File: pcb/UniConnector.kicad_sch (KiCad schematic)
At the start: 1 part

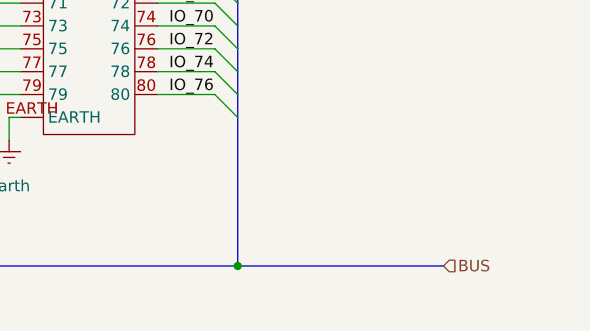
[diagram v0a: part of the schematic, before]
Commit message: Add junction and bus entries to UniConnector schematic
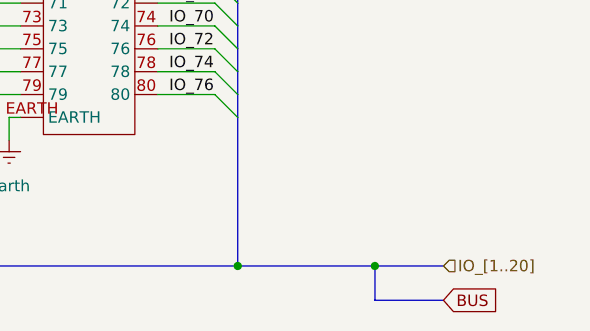
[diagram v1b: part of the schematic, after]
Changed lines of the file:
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@@
 		(color 0 0 0 0)
 	)
+	(junction
+		(at 138.43 146.05)
+		(diameter 0)
+		(color 0 0 0 0)
+	)
 	(bus_entry
 		(at 90.17 124.46)
@@
 		)
 	)
+	(bus
+		(pts
+			(xy 138.43 149.86) (xy 146.05 149.86)
+		)
+		(stroke
+			(width 0)
+			(type default)
+		)
+	)
 	(wire
 		(pts
@@
 		)
 	)
+	(bus
+		(pts
+			(xy 138.43 146.05) (xy 146.05 146.05)
+		)
+		(stroke
+			(width 0)
+			(type default)
+		)
+	)
 	(wire
 		(pts
@@
 	(bus
 		(pts
-			(xy 123.19 146.05) (xy 146.05 146.05)
+			(xy 123.19 146.05) (xy 138.43 146.05)
 		)
 		(stroke
@@
 		(pts
 			(xy 114.3 40.64) (xy 120.65 40.64)
+		)
+		(stroke
+			(width 0)
+			(type default)
+		)
+	)
+	(bus
+		(pts
+			(xy 138.43 146.05) (xy 138.43 149.86)
 		)
 		(stroke
@@
 		)
 	)
-	(hierarchical_label "BUS"
+	(global_label "BUS"
+		(shape input)
+		(at 146.05 149.86 0)
+		(fields_autoplaced yes)
+		(effects
+			(font
+				(size 1.27 1.27)
+			)
+			(justify left)
+		)
+		(property "Intersheetrefs" "${INTERSHEET_REFS}"
+			(at 152.191 149.86 0)
+			(effects
+				(font
+					(size 1.27 1.27)
+				)
+				(justify left)
+				(hide yes)
+			)
+		)
+	)
+	(hierarchical_label "IO_[1..20]"
 		(shape input)
 		(at 146.05 146.05 0)

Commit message: UniConnector new traces
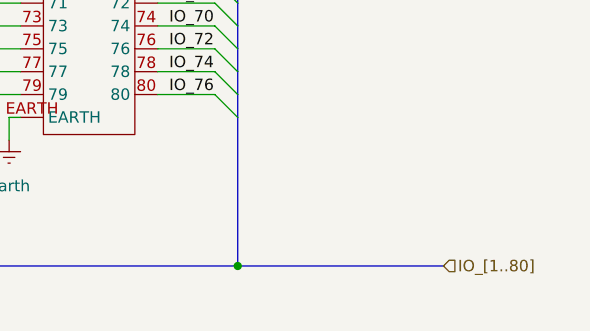
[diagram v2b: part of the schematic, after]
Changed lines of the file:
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@@
 		(color 0 0 0 0)
 	)
-	(junction
-		(at 138.43 146.05)
-		(diameter 0)
-		(color 0 0 0 0)
-	)
 	(bus_entry
 		(at 90.17 124.46)
@@
 		)
 	)
-	(bus
-		(pts
-			(xy 138.43 149.86) (xy 146.05 149.86)
-		)
-		(stroke
-			(width 0)
-			(type default)
-		)
-	)
 	(wire
 		(pts
@@
 		)
 	)
-	(bus
-		(pts
-			(xy 138.43 146.05) (xy 146.05 146.05)
-		)
-		(stroke
-			(width 0)
-			(type default)
-		)
-	)
 	(wire
 		(pts
@@
 	(bus
 		(pts
-			(xy 123.19 146.05) (xy 138.43 146.05)
+			(xy 123.19 146.05) (xy 146.05 146.05)
 		)
 		(stroke
@@
 		(pts
 			(xy 114.3 40.64) (xy 120.65 40.64)
-		)
-		(stroke
-			(width 0)
-			(type default)
-		)
-	)
-	(bus
-		(pts
-			(xy 138.43 146.05) (xy 138.43 149.86)
 		)
 		(stroke
@@
 		)
 	)
-	(global_label "BUS"
-		(shape input)
-		(at 146.05 149.86 0)
-		(fields_autoplaced yes)
-		(effects
-			(font
-				(size 1.27 1.27)
-			)
-			(justify left)
-		)
-		(property "Intersheetrefs" "${INTERSHEET_REFS}"
-			(at 152.191 149.86 0)
-			(effects
-				(font
-					(size 1.27 1.27)
-				)
-				(justify left)
-				(hide yes)
-			)
-		)
-	)
-	(hierarchical_label "IO_[1..20]"
+	(hierarchical_label "IO_[1..80]"
 		(shape input)
 		(at 146.05 146.05 0)

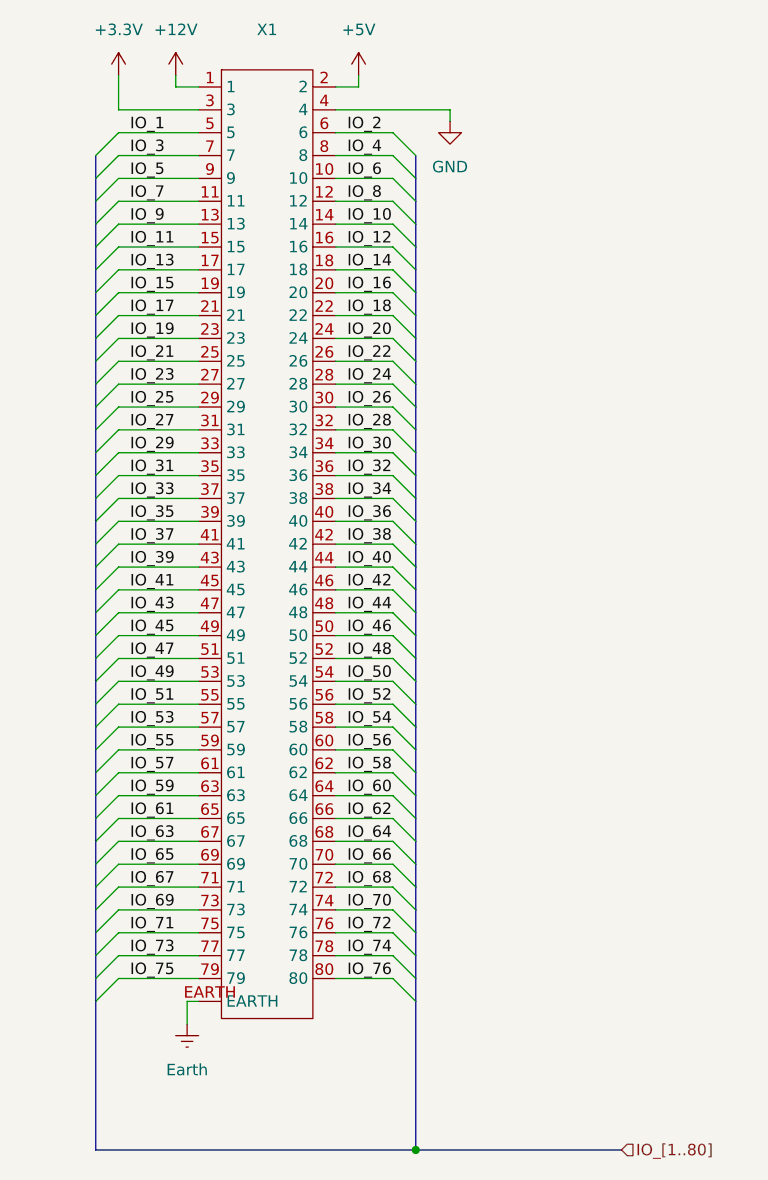
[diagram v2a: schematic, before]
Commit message: Added SI5351C
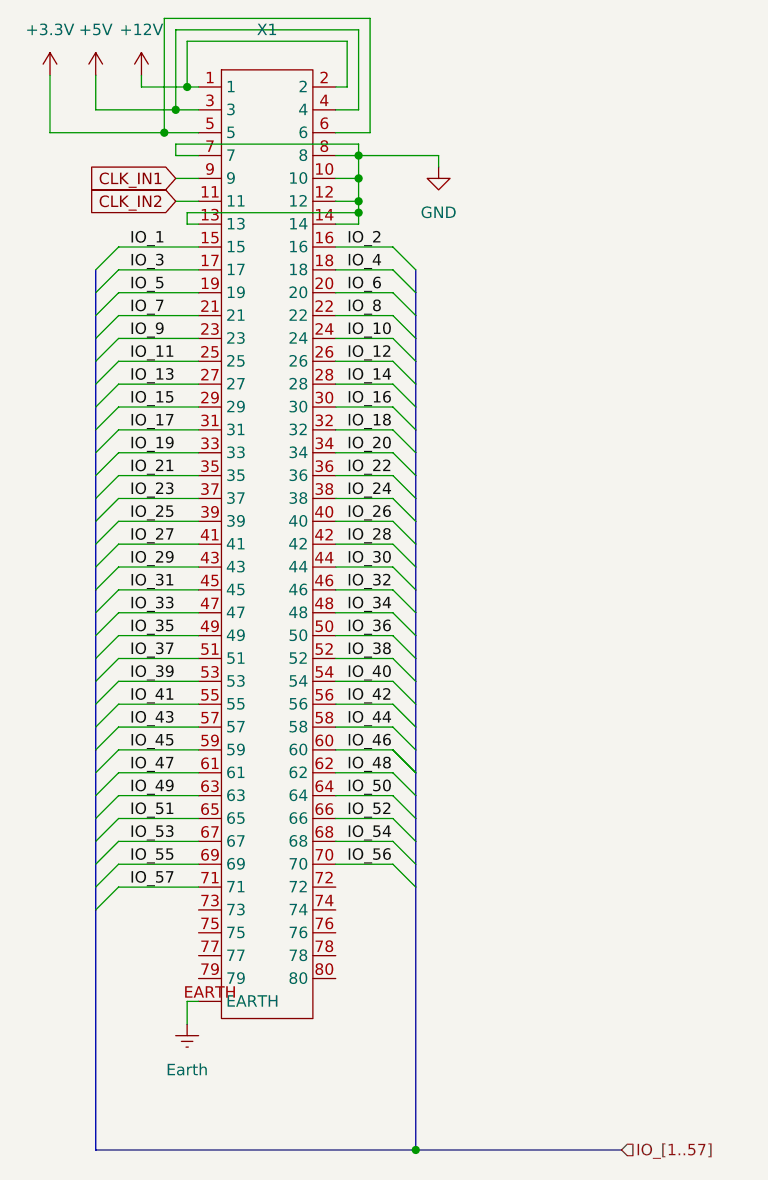
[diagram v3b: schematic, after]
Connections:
- net IO_58 is gone; now on net IO_48: X1.62
- net IO_59 is gone; now on net IO_49: X1.63
- net IO_60 is gone; now on net IO_50: X1.64
- net IO_61 is gone; now on net IO_51: X1.65
- net IO_62 is gone; now on net IO_52: X1.66
- net IO_63 is gone; now on net IO_53: X1.67
- net IO_64 is gone; now on net IO_54: X1.68
- net IO_65 is gone; now on net IO_55: X1.69
- net IO_66 is gone; now on net IO_56: X1.70
- net IO_67 is gone; now on net IO_57: X1.71
- net +12V: now also X1.2
- net +3.3V: now also X1.5, X1.6; no longer X1.3
- net +5V: now also X1.3, X1.4; no longer X1.2
- net GND: now also X1.10, X1.12, X1.13, X1.14, X1.7, X1.8; no longer X1.4
- net IO_1: now also X1.15; no longer X1.5
- net IO_10: now also X1.24; no longer X1.14
- net IO_11: now also X1.25; no longer X1.15
- net IO_12: now also X1.26; no longer X1.16
- net IO_13: now also X1.27; no longer X1.17
- net IO_14: now also X1.28; no longer X1.18
- net IO_15: now also X1.29; no longer X1.19
- net IO_16: now also X1.30; no longer X1.20
- net IO_17: now also X1.31; no longer X1.21
- net IO_18: now also X1.32; no longer X1.22
- net IO_19: now also X1.33; no longer X1.23
- net IO_2: now also X1.16; no longer X1.6
- net IO_20: now also X1.34; no longer X1.24
- net IO_21: now also X1.35; no longer X1.25
- net IO_22: now also X1.36; no longer X1.26
- net IO_23: now also X1.37; no longer X1.27
- net IO_24: now also X1.38; no longer X1.28
- net IO_25: now also X1.39; no longer X1.29
- net IO_26: now also X1.40; no longer X1.30
- net IO_27: now also X1.41; no longer X1.31
- net IO_28: now also X1.42; no longer X1.32
- net IO_29: now also X1.43; no longer X1.33
- net IO_3: now also X1.17; no longer X1.7
- net IO_30: now also X1.44; no longer X1.34
- net IO_31: now also X1.45; no longer X1.35
- net IO_32: now also X1.46; no longer X1.36
- net IO_33: now also X1.47; no longer X1.37
- net IO_34: now also X1.48; no longer X1.38
- net IO_35: now also X1.49; no longer X1.39
- net IO_36: now also X1.50; no longer X1.40
- net IO_37: now also X1.51; no longer X1.41
- net IO_38: now also X1.52; no longer X1.42
- net IO_39: now also X1.53; no longer X1.43
- net IO_4: now also X1.18; no longer X1.8
- net IO_40: now also X1.54; no longer X1.44
- net IO_41: now also X1.55; no longer X1.45
- net IO_42: now also X1.56; no longer X1.46
- net IO_43: now also X1.57; no longer X1.47
- net IO_44: now also X1.58; no longer X1.48
- net IO_45: now also X1.59; no longer X1.49
- net IO_46: now also X1.60; no longer X1.50
- net IO_47: now also X1.61; no longer X1.51
- net IO_48: no longer X1.52
- net IO_49: no longer X1.53
- net IO_5: now also X1.19; no longer X1.9
- net IO_50: no longer X1.54
- net IO_51: no longer X1.55
- net IO_52: no longer X1.56
- net IO_53: no longer X1.57
- net IO_54: no longer X1.58
- net IO_55: no longer X1.59
- net IO_56: no longer X1.60
- net IO_57: no longer X1.61
- net IO_6: now also X1.20; no longer X1.10
- net IO_7: now also X1.21; no longer X1.11
- net IO_8: now also X1.22; no longer X1.12
- net IO_9: now also X1.23; no longer X1.13
- net IO_68: no longer names the net of X1.72
- net IO_69: no longer names the net of X1.73
- net IO_70: no longer names the net of X1.74
- net IO_71: no longer names the net of X1.75
- net IO_72: no longer names the net of X1.76
- net IO_73: no longer names the net of X1.77
- net IO_74: no longer names the net of X1.78
- net IO_75: no longer names the net of X1.79
- net IO_76: no longer names the net of X1.80
- new net CLK_IN1: X1.9
- new net CLK_IN2: X1.11

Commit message: Clock rounting
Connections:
- net CLK_IN1: now also X1.11; no longer X1.9
- net CLK_IN2: now also X1.9; no longer X1.11
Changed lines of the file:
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@@
 		)
 	)
-	(global_label "CLK_IN1"
+	(hierarchical_label "CLK_IN1"
 		(shape input)
-		(at 96.52 38.1 180)
-		(fields_autoplaced yes)
+		(at 96.52 40.64 180)
 		(effects
 			(font
@@
 			(justify right)
 		)
-		(property "Intersheetrefs" "${INTERSHEET_REFS}"
-			(at 86.5085 38.1 0)
-			(effects
-				(font
-					(size 1.27 1.27)
-				)
-				(justify right)
-				(hide yes)
-			)
-		)
 	)
-	(global_label "CLK_IN2"
+	(hierarchical_label "CLK_IN2"
 		(shape input)
-		(at 96.52 40.64 180)
-		(fields_autoplaced yes)
+		(at 96.52 38.1 180)
 		(effects
 			(font
@@
 			(justify right)
 		)
-		(property "Intersheetrefs" "${INTERSHEET_REFS}"
-			(at 86.5085 40.64 0)
-			(effects
-				(font
-					(size 1.27 1.27)
-				)
-				(justify right)
-				(hide yes)
-			)
-		)
 	)

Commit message: New routing
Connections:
- net CLK_IN1: now also X1.13; no longer X1.11
- net CLK_IN2: now also X1.11; no longer X1.9
- net GND: now also X1.15, X1.16, X1.9; no longer X1.13, X1.7, X1.8
- net IO_1: now also X1.17; no longer X1.15
- net IO_10: now also X1.26; no longer X1.24
- net IO_11: now also X1.27; no longer X1.25
- net IO_12: now also X1.28; no longer X1.26
- net IO_13: now also X1.29; no longer X1.27
- net IO_14: now also X1.30; no longer X1.28
- net IO_15: now also X1.31; no longer X1.29
- net IO_16: now also X1.32; no longer X1.30
- net IO_17: now also X1.33; no longer X1.31
- net IO_18: now also X1.34; no longer X1.32
- net IO_19: now also X1.35; no longer X1.33
- net IO_2: now also X1.18; no longer X1.16
- net IO_20: now also X1.36; no longer X1.34
- net IO_21: now also X1.37; no longer X1.35
- net IO_22: now also X1.38; no longer X1.36
- net IO_23: now also X1.39; no longer X1.37
- net IO_24: now also X1.40; no longer X1.38
- net IO_25: now also X1.41; no longer X1.39
- net IO_26: now also X1.42; no longer X1.40
- net IO_27: now also X1.43; no longer X1.41
- net IO_28: now also X1.44; no longer X1.42
- net IO_29: now also X1.45; no longer X1.43
- net IO_3: now also X1.19; no longer X1.17
- net IO_30: now also X1.46; no longer X1.44
- net IO_31: now also X1.47; no longer X1.45
- net IO_32: now also X1.48; no longer X1.46
- net IO_33: now also X1.49; no longer X1.47
- net IO_34: now also X1.50; no longer X1.48
- net IO_35: now also X1.51; no longer X1.49
- net IO_36: now also X1.52; no longer X1.50
- net IO_37: now also X1.53; no longer X1.51
- net IO_38: now also X1.54; no longer X1.52
- net IO_39: now also X1.55; no longer X1.53
- net IO_4: now also X1.20; no longer X1.18
- net IO_40: now also X1.56; no longer X1.54
- net IO_41: now also X1.57; no longer X1.55
- net IO_42: now also X1.58; no longer X1.56
- net IO_43: now also X1.59; no longer X1.57
- net IO_44: now also X1.60; no longer X1.58
- net IO_45: now also X1.61; no longer X1.59
- net IO_46: now also X1.62; no longer X1.60
- net IO_47: now also X1.63; no longer X1.61
- net IO_48: now also X1.64; no longer X1.62
- net IO_49: now also X1.65; no longer X1.63
- net IO_5: now also X1.21; no longer X1.19
- net IO_50: now also X1.66; no longer X1.64
- net IO_51: now also X1.67; no longer X1.65
- net IO_52: now also X1.68; no longer X1.66
- net IO_53: now also X1.69; no longer X1.67
- net IO_54: now also X1.70; no longer X1.68
- net IO_55: now also X1.71; no longer X1.69
- net IO_56: now also X1.72; no longer X1.70
- net IO_57: now also X1.73; no longer X1.71
- net IO_6: now also X1.22; no longer X1.20
- net IO_7: now also X1.23; no longer X1.21
- net IO_8: now also X1.24; no longer X1.22
- net IO_9: now also X1.25; no longer X1.23
- new net -12V: X1.7, X1.8

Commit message: More routing
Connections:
- net GND: now also X1.74, X1.75, X1.76, X1.77, X1.78, X1.79, X1.80
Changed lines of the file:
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@@
+	)
+	(junction
+		(at 116.84 121.92)
+		(diameter 0)
+		(color 0 0 0 0)
 	)
 	(junction
@@
 	)
 	(junction
+		(at 92.71 127)
+		(diameter 0)
+		(color 0 0 0 0)
+	)
+	(junction
+		(at 92.71 124.46)
+		(diameter 0)
+		(color 0 0 0 0)
+	)
+	(junction
 		(at 96.52 30.48)
+		(diameter 0)
+		(color 0 0 0 0)
+	)
+	(junction
+		(at 116.84 127)
 		(diameter 0)
 		(color 0 0 0 0)
@@
 	)
 	(junction
+		(at 116.84 124.46)
+		(diameter 0)
+		(color 0 0 0 0)
+	)
+	(junction
 		(at 123.19 148.59)
 		(diameter 0)
@@
 	)
 	(junction
+		(at 116.84 142.24)
+		(diameter 0)
+		(color 0 0 0 0)
+	)
+	(junction
 		(at 95.25 33.02)
 		(diameter 0)
@@
 	(wire
 		(pts
+			(xy 116.84 142.24) (xy 116.84 127)
+		)
+		(stroke
+			(width 0)
+			(type default)
+		)
+	)
+	(wire
+		(pts
 			(xy 90.17 78.74) (xy 99.06 78.74)
 		)
@@
 	(wire
 		(pts
+			(xy 99.06 121.92) (xy 92.71 121.92)
+		)
+		(stroke
+			(width 0)
+			(type default)
+		)
+	)
+	(wire
+		(pts
 			(xy 90.17 19.05) (xy 90.17 35.56)
 		)
@@
 		)
 	)
+	(wire
+		(pts
+			(xy 92.71 127) (xy 99.06 127)
+		)
+		(stroke
+			(width 0)
+			(type default)
+		)
+	)
+	(wire
+		(pts
+			(xy 114.3 121.92) (xy 116.84 121.92)
+		)
+		(stroke
+			(width 0)
+			(type default)
+		)
+	)
+	(wire
+		(pts
+			(xy 92.71 142.24) (xy 116.84 142.24)
+		)
+		(stroke
+			(width 0)
+			(type default)
+		)
+	)
 	(bus
 		(pts
@@
 	(wire
 		(pts
+			(xy 92.71 124.46) (xy 92.71 127)
+		)
+		(stroke
+			(width 0)
+			(type default)
+		)
+	)
+	(wire
+		(pts
 			(xy 114.3 111.76) (xy 120.65 111.76)
 		)
@@
 	(wire
 		(pts
+			(xy 116.84 142.24) (xy 116.84 144.78)
+		)
+		(stroke
+			(width 0)
+			(type default)
+		)
+	)
+	(wire
+		(pts
 			(xy 114.3 60.96) (xy 120.65 60.96)
 		)
@@
 	(wire
 		(pts
+			(xy 114.3 127) (xy 116.84 127)
+		)
+		(stroke
+			(width 0)
+			(type default)
+		)
+	)
+	(wire
+		(pts
 			(xy 114.3 73.66) (xy 120.65 73.66)
 		)
@@
 	(wire
 		(pts
+			(xy 116.84 124.46) (xy 116.84 121.92)
+		)
+		(stroke
+			(width 0)
+			(type default)
+		)
+	)
+	(wire
+		(pts
 			(xy 114.3 88.9) (xy 120.65 88.9)
 		)
@@
 	(wire
 		(pts
+			(xy 116.84 119.38) (xy 114.3 119.38)
+		)
+		(stroke
+			(width 0)
+			(type default)
+		)
+	)
+	(wire
+		(pts
 			(xy 90.17 99.06) (xy 99.06 99.06)
 		)
@@
 	(wire
 		(pts
+			(xy 92.71 121.92) (xy 92.71 124.46)
+		)
+		(stroke
+			(width 0)
+			(type default)
+		)
+	)
+	(wire
+		(pts
 			(xy 97.79 27.94) (xy 97.79 22.86)
 		)
@@
 	(wire
 		(pts
+			(xy 92.71 124.46) (xy 99.06 124.46)
+		)
+		(stroke
+			(width 0)
+			(type default)
+		)
+	)
+	(wire
+		(pts
 			(xy 90.17 114.3) (xy 99.06 114.3)
 		)
@@
 	(wire
 		(pts
+			(xy 114.3 124.46) (xy 116.84 124.46)
+		)
+		(stroke
+			(width 0)
+			(type default)
+		)
+	)
+	(wire
+		(pts
 			(xy 90.17 68.58) (xy 99.06 68.58)
 		)
@@
 	(wire
 		(pts
+			(xy 116.84 127) (xy 116.84 124.46)
+		)
+		(stroke
+			(width 0)
+			(type default)
+		)
+	)
+	(wire
+		(pts
 			(xy 90.17 111.76) (xy 99.06 111.76)
 		)
@@
 		)
 	)
+	(wire
+		(pts
+			(xy 92.71 127) (xy 92.71 142.24)
+		)
+		(stroke
+			(width 0)
+			(type default)
+		)
+	)
 	(bus
 		(pts
@@
 		(pts
 			(xy 114.3 48.26) (xy 120.65 48.26)
+		)
+		(stroke
+			(width 0)
+			(type default)
+		)
+	)
+	(wire
+		(pts
+			(xy 116.84 121.92) (xy 116.84 119.38)
 		)
 		(stroke
@@
 		)
 	)
+	(symbol
+		(lib_id "power:GND")
+		(at 116.84 144.78 0)
+		(mirror y)
+		(unit 1)
+		(exclude_from_sim no)
+		(in_bom yes)
+		(on_board yes)
+		(dnp no)
+		(fields_autoplaced yes)
+		(property "Reference" "#PWR057"
+			(at 116.84 151.13 0)
+			(effects
+				(font
+					(size 1.27 1.27)
+				)
+				(hide yes)
+			)
+		)
+		(property "Value" "GND"
+			(at 116.84 149.86 0)
+			(effects
+				(font
+					(size 1.27 1.27)
+				)
+			)
+		)
+		(property "Footprint" ""
+			(at 116.84 144.78 0)
+			(effects
+				(font
+					(size 1.27 1.27)
+				)
+				(hide yes)
+			)
+		)
+		(property "Datasheet" ""
+			(at 116.84 144.78 0)
+			(effects
+				(font
+					(size 1.27 1.27)
+				)
+				(hide yes)
+			)
+		)
+		(property "Description" "Power symbol creates a global label with name \"GND\" , ground"
+			(at 116.84 144.78 0)
+			(effects
+				(font
+					(size 1.27 1.27)
+				)
+				(hide yes)
+			)
+		)
+		(pin "1"
+		)
+		(instances
+			(project "UCB_board"
+				(path "/0c4edb77-9bdf-4103-be66-c5eb9940b163/979aab86-2332-41e6-a643-ae3ec5ef42ab"
+					(reference "#PWR057")
+					(unit 1)
+				)
+			)
+		)
+	)
